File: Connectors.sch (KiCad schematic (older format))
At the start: 4 parts

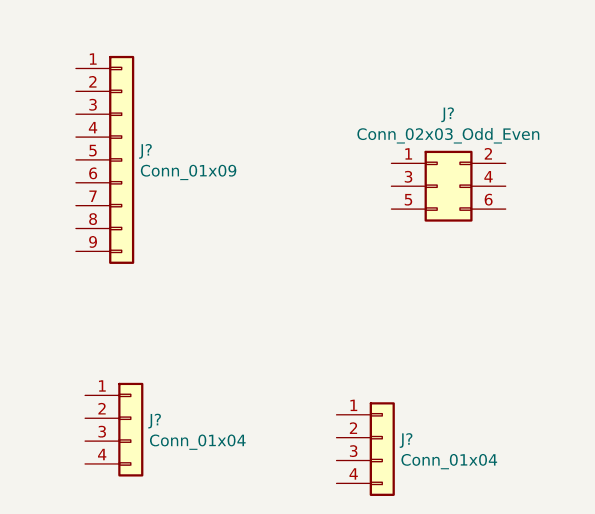
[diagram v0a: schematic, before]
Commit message: footprints associated to symbols
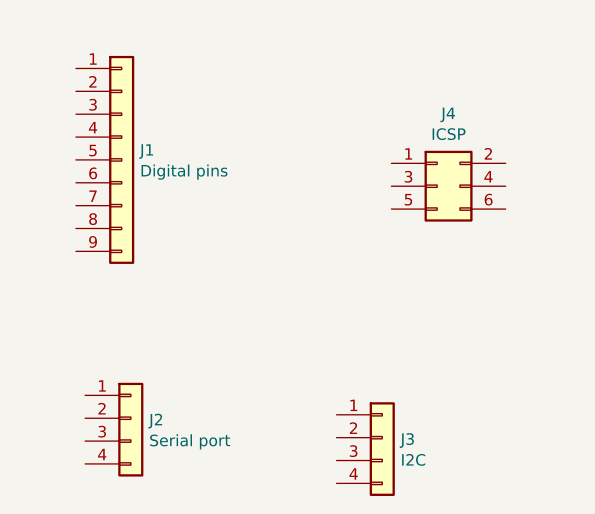
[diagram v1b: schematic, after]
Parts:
- J1: renamed from J?; value Conn_01x09 -> Digital pins; footprint (none) -> Connector_PinSocket_2.54mm:PinSocket_1x09_P2.54mm_Vertical
- J2: renamed from J?; value Conn_01x04 -> Serial port; footprint (none) -> Connector_PinSocket_2.54mm:PinSocket_1x04_P2.54mm_Vertical
- J3: renamed from J?; value Conn_01x04 -> I2C; footprint (none) -> Connector_PinSocket_2.54mm:PinSocket_1x04_P2.54mm_Vertical
- J4: renamed from J?; value Conn_02x03_Odd_Even -> ICSP; footprint (none) -> Connector_PinSocket_2.54mm:PinSocket_2x03_P2.54mm_Vertical
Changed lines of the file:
@@
 $EndDescr
 $Comp
-L Connector_Generic:Conn_02x03_Odd_Even J?
+L Connector_Generic:Conn_02x03_Odd_Even J4
 U 1 1 5FC2F982
 P 5010 2560
-F 0 "J?" H 5060 2877 50  0000 C CNN
-F 1 "Conn_02x03_Odd_Even" H 5060 2786 50  0000 C CNN
-F 2 "" H 5010 2560 50  0001 C CNN
+F 0 "J4" H 5060 2877 50  0000 C CNN
+F 1 "ICSP" H 5060 2786 50  0000 C CNN
+F 2 "Connector_PinSocket_2.54mm:PinSocket_2x03_P2.54mm_Vertical" H 5010 2560 50  0001 C CNN
 F 3 "~" H 5010 2560 50  0001 C CNN
 	1    5010 2560
@@
 $EndComp
 $Comp
-L Connector_Generic:Conn_01x09 J?
+L Connector_Generic:Conn_01x09 J1
 U 1 1 5FC30DE1
 P 3630 2445
-F 0 "J?" H 3710 2487 50  0000 L CNN
-F 1 "Conn_01x09" H 3710 2396 50  0000 L CNN
-F 2 "" H 3630 2445 50  0001 C CNN
+F 0 "J1" H 3710 2487 50  0000 L CNN
+F 1 "Digital pins" H 3710 2396 50  0000 L CNN
+F 2 "Connector_PinSocket_2.54mm:PinSocket_1x09_P2.54mm_Vertical" H 3630 2445 50  0001 C CNN
 F 3 "~" H 3630 2445 50  0001 C CNN
 	1    3630 2445
@@
 $EndComp
 $Comp
-L Connector_Generic:Conn_01x04 J?
+L Connector_Generic:Conn_01x04 J2
 U 1 1 5FC31E17
 P 3670 3575
-F 0 "J?" H 3750 3567 50  0000 L CNN
-F 1 "Conn_01x04" H 3750 3476 50  0000 L CNN
-F 2 "" H 3670 3575 50  0001 C CNN
+F 0 "J2" H 3750 3567 50  0000 L CNN
+F 1 "Serial port" H 3750 3476 50  0000 L CNN
+F 2 "Connector_PinSocket_2.54mm:PinSocket_1x04_P2.54mm_Vertical" H 3670 3575 50  0001 C CNN
 F 3 "~" H 3670 3575 50  0001 C CNN
 	1    3670 3575
@@
 $EndComp
 $Comp
-L Connector_Generic:Conn_01x04 J?
+L Connector_Generic:Conn_01x04 J3
 U 1 1 5FC3248B
 P 4770 3660
-F 0 "J?" H 4850 3652 50  0000 L CNN
-F 1 "Conn_01x04" H 4850 3561 50  0000 L CNN
-F 2 "" H 4770 3660 50  0001 C CNN
+F 0 "J3" H 4850 3652 50  0000 L CNN
+F 1 "I2C" H 4850 3561 50  0000 L CNN
+F 2 "Connector_PinSocket_2.54mm:PinSocket_1x04_P2.54mm_Vertical" H 4770 3660 50  0001 C CNN
 F 3 "~" H 4770 3660 50  0001 C CNN
 	1    4770 3660

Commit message: finished schematics with comments
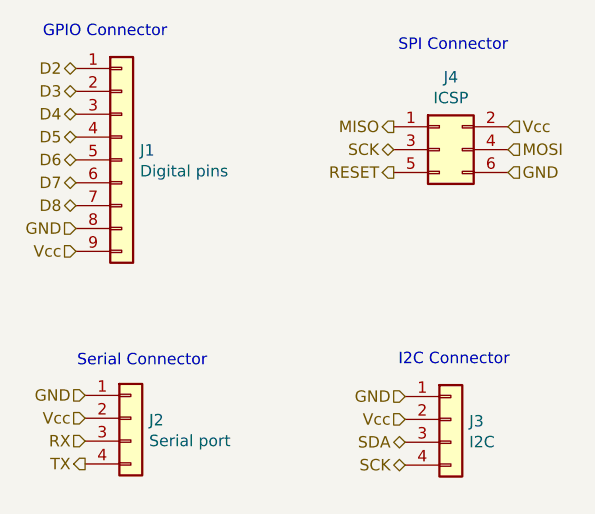
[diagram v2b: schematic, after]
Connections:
- net MISO: now reaches J4.1 (Pin_1)
- net Vcc: now reaches J4.2 (Pin_2)
- net Vcc: now also J1.9 (Pin_9), J2.2 (Pin_2), J3.2 (Pin_2)
- net SCK: now reaches J4.3 (Pin_3)
- net SCK: now also J3.4 (Pin_4)
- net MOSI: now reaches J4.4 (Pin_4)
- net RESET: now reaches J4.5 (Pin_5)
- net GND: now reaches J4.6 (Pin_6)
- net GND: now also J1.8 (Pin_8), J2.1 (Pin_1), J3.1 (Pin_1)
- net D2: now reaches J1.1 (Pin_1)
- net D3: now reaches J1.2 (Pin_2)
- net D4: now reaches J1.3 (Pin_3)
- net D5: now reaches J1.4 (Pin_4)
- net D6: now reaches J1.5 (Pin_5)
- net D7: now reaches J1.6 (Pin_6)
- net D8: now reaches J1.7 (Pin_7)
- net RX: now reaches J2.3 (Pin_3)
- net TX: now reaches J2.4 (Pin_4)
- net SDA: now reaches J3.3 (Pin_3)
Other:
- note added: "GPIO Connector"
- note added: "I2C Connector"
- note added: "SPI Connector"
- note added: "Serial Connector"
- moved on the sheet: J3, J4
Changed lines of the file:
@@
 L Connector_Generic:Conn_02x03_Odd_Even J4
 U 1 1 5FC2F982
-P 5010 2560
-F 0 "J4" H 5060 2877 50  0000 C CNN
-F 1 "ICSP" H 5060 2786 50  0000 C CNN
-F 2 "Connector_PinSocket_2.54mm:PinSocket_2x03_P2.54mm_Vertical" H 5010 2560 50  0001 C CNN
-F 3 "~" H 5010 2560 50  0001 C CNN
-	1    5010 2560
+P 5020 2400
+F 0 "J4" H 5070 2717 50  0000 C CNN
+F 1 "ICSP" H 5070 2626 50  0000 C CNN
+F 2 "Connector_PinSocket_2.54mm:PinSocket_2x03_P2.54mm_Vertical" H 5020 2400 50  0001 C CNN
+F 3 "~" H 5020 2400 50  0001 C CNN
+	1    5020 2400
 	1    0    0    -1
 $EndComp
@@
 L Connector_Generic:Conn_01x04 J3
 U 1 1 5FC3248B
-P 4770 3660
-F 0 "J3" H 4850 3652 50  0000 L CNN
-F 1 "I2C" H 4850 3561 50  0000 L CNN
-F 2 "Connector_PinSocket_2.54mm:PinSocket_1x04_P2.54mm_Vertical" H 4770 3660 50  0001 C CNN
-F 3 "~" H 4770 3660 50  0001 C CNN
-	1    4770 3660
+P 5070 3580
+F 0 "J3" H 5150 3572 50  0000 L CNN
+F 1 "I2C" H 5150 3481 50  0000 L CNN
+F 2 "Connector_PinSocket_2.54mm:PinSocket_1x04_P2.54mm_Vertical" H 5070 3580 50  0001 C CNN
+F 3 "~" H 5070 3580 50  0001 C CNN
+	1    5070 3580
 	1    0    0    -1
 $EndComp
+Text HLabel 4820 2300 0    50   Output ~ 0
+MISO
+Text HLabel 4820 2400 0    50   BiDi ~ 0
+SCK
+Text HLabel 5320 2300 2    50   Input ~ 0
+Vcc
+Text HLabel 5320 2400 2    50   Input ~ 0
+MOSI
+Text HLabel 5320 2500 2    50   Input ~ 0
+GND
+Text HLabel 4820 2500 0    50   Output ~ 0
+RESET
+Text HLabel 3470 3475 0    50   Input ~ 0
+GND
+Text HLabel 3470 3575 0    50   Input ~ 0
+Vcc
+Text HLabel 3470 3675 0    50   Input ~ 0
+RX
+Text HLabel 3470 3775 0    50   Output ~ 0
+TX
+Text HLabel 4870 3480 0    50   Input ~ 0
+GND
+Text HLabel 4870 3580 0    50   Input ~ 0
+Vcc
+Text HLabel 4870 3680 0    50   BiDi ~ 0
+SDA
+Text HLabel 4870 3780 0    50   BiDi ~ 0
+SCK
+Text HLabel 3430 2045 0    50   BiDi ~ 0
+D2
+Text HLabel 3430 2145 0    50   BiDi ~ 0
+D3
+Text HLabel 3430 2245 0    50   BiDi ~ 0
+D4
+Text HLabel 3430 2345 0    50   BiDi ~ 0
+D5
+Text HLabel 3430 2445 0    50   BiDi ~ 0
+D6
+Text HLabel 3430 2545 0    50   BiDi ~ 0
+D7
+Text HLabel 3430 2645 0    50   BiDi ~ 0
+D8
+Text HLabel 3430 2745 0    50   Input ~ 0
+GND
+Text HLabel 3430 2845 0    50   Input ~ 0
+Vcc
+Text Notes 4840 1975 0    50   ~ 0
+SPI Connector
+Text Notes 4840 3350 0    50   ~ 0
+I2C Connector
+Text Notes 3435 3355 0    50   ~ 0
+Serial Connector
+Text Notes 3285 1915 0    50   ~ 0
+GPIO Connector
 $EndSCHEMATC
